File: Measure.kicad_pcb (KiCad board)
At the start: 4 copper layers, 68.1 x 46 mm, 34 parts, among them J1 Input, J2 Output, J3 +5V, U1 TMR_1-0511

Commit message: Первая версия в производство
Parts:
- added H1: MountingHole, MountingHole:MountingHole_3.2mm_M3, F.Cu at (126.2, 65.0)
- added H2: MountingHole, MountingHole:MountingHole_3.2mm_M3, F.Cu at (186.7, 65.0)
- added H3: MountingHole, MountingHole:MountingHole_3.2mm_M3, F.Cu at (126.2, 103.4)
- added H4: MountingHole, MountingHole:MountingHole_3.2mm_M3, F.Cu at (186.7, 103.4)
- moved J3 8.00 mm to (180.6, 73.8)
- moved J1 2.96 mm to (134.1, 71.2), turned to 0 degrees
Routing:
- net /Voltage_OUT: track 14.5 -> 4.61 mm
- net /Voltage_IN: track 28.3 -> 23.5 mm
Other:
- board text added: "+"
- board text added: "+5V"
- board text added: "-"
- board text added: "IN VM"
- board text added: "Input"
- board text added: "OUT VM"
- board text added: "V_IN"
- board text added: "V_OUT"

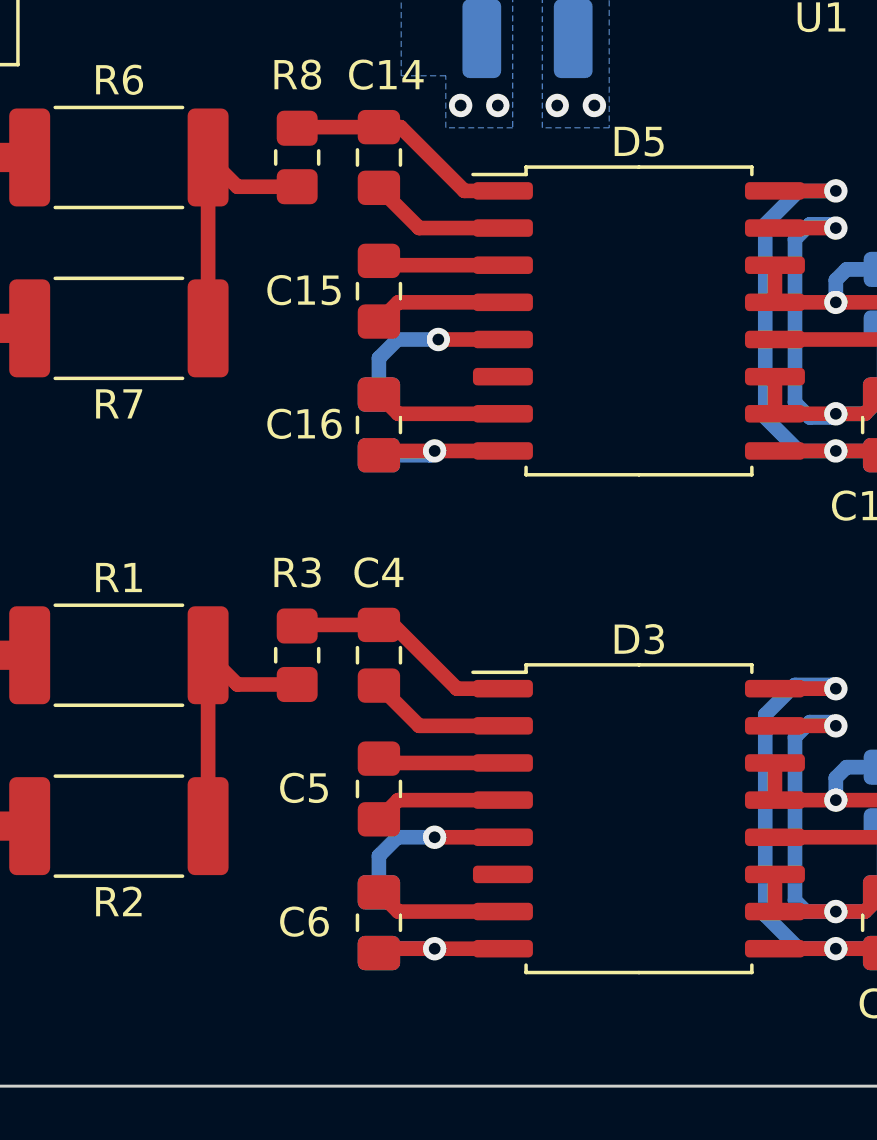
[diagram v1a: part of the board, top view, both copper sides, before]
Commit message: Исправлены ошибки с неподключённым IN- и питанием
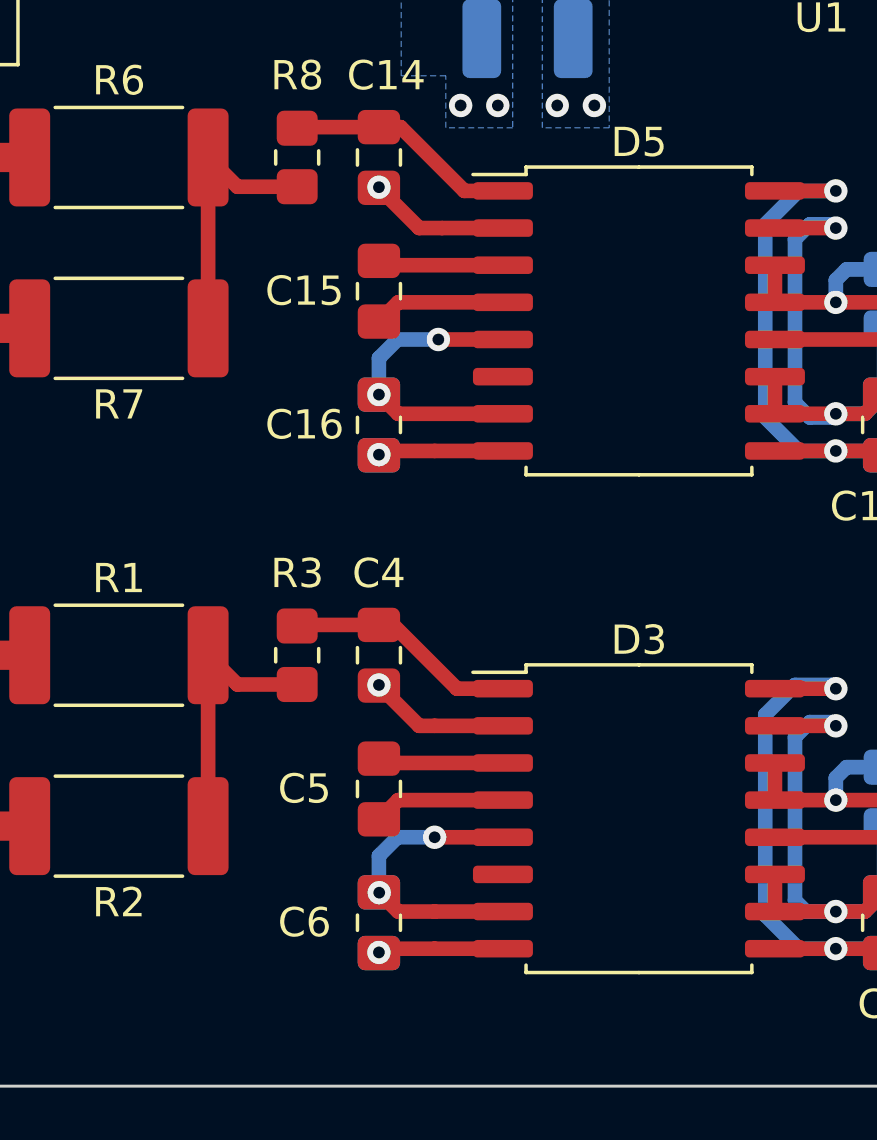
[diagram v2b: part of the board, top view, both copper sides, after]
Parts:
- C13, C2: value C_Small -> 1u
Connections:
- C14 pad 2: Net-(C14-Pad2) -> GNDPWR
- C16 pad 1: Net-(C16-Pad1) -> +5VP
- C4 pad 2: Net-(C4-Pad2) -> GNDPWR
- C6 pad 1: Net-(C6-Pad1) -> +5VP
- D3 pad 2: Net-(C4-Pad2) -> GNDPWR
- D3 pad 7: Net-(C6-Pad1) -> +5VP
- D5 pad 2: Net-(C14-Pad2) -> GNDPWR
- D5 pad 7: Net-(C16-Pad1) -> +5VP
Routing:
- net +5VP: track 11.5 -> 20.5 mm, vias 4 -> 6
- net GNDPWR: track 17.9 -> 23.6 mm, vias 6 -> 8
- net Net-(C4-Pad2): track 4.81 -> 0.00 mm
- net Net-(C14-Pad2): track 4.81 -> 0.00 mm
- net Net-(C6-Pad1): track 4.51 -> 0.00 mm
- net Net-(C16-Pad1): track 4.51 -> 0.00 mm
